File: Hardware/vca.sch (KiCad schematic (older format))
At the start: 0 parts

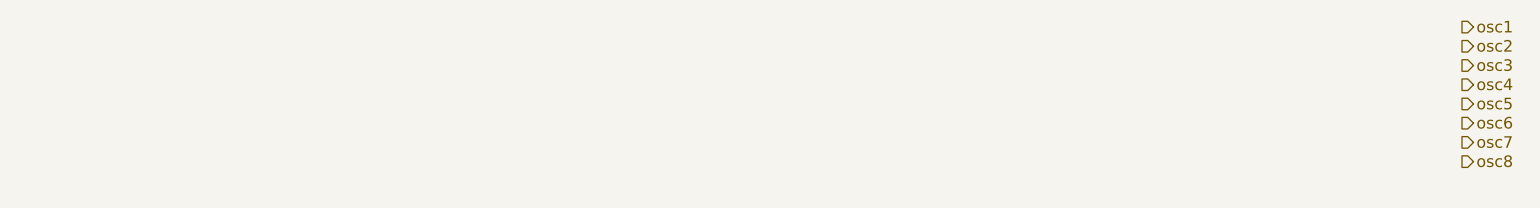
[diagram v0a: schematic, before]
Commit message: add sheets for the remaining functionality. This should hopefully be all sheets, but might add more if necessary.
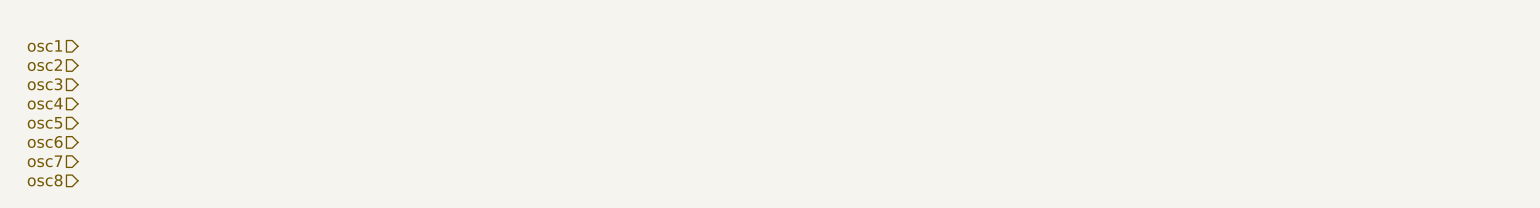
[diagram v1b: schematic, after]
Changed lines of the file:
@@
 $Descr A4 11693 8268
 encoding utf-8
-Sheet 2 7
+Sheet 5 7
 Title ""
 Date ""
@@
 Comment4 ""
 $EndDescr
-Text HLabel 9050 1900 2    60   Output ~ 0
+Text HLabel 1850 2000 0    60   Input ~ 0
 osc1
-Text HLabel 9050 2000 2    60   Output ~ 0
+Text HLabel 1850 2100 0    60   Input ~ 0
 osc2
-Text HLabel 9050 2100 2    60   Output ~ 0
+Text HLabel 1850 2200 0    60   Input ~ 0
 osc3
-Text HLabel 9050 2200 2    60   Output ~ 0
+Text HLabel 1850 2300 0    60   Input ~ 0
 osc4
-Text HLabel 9050 2300 2    60   Output ~ 0
+Text HLabel 1850 2400 0    60   Input ~ 0
 osc5
-Text HLabel 9050 2400 2    60   Output ~ 0
+Text HLabel 1850 2500 0    60   Input ~ 0
 osc6
-Text HLabel 9050 2500 2    60   Output ~ 0
+Text HLabel 1850 2600 0    60   Input ~ 0
 osc7
-Text HLabel 9050 2600 2    60   Output ~ 0
+Text HLabel 1850 2700 0    60   Input ~ 0
 osc8
 $EndSCHEMATC

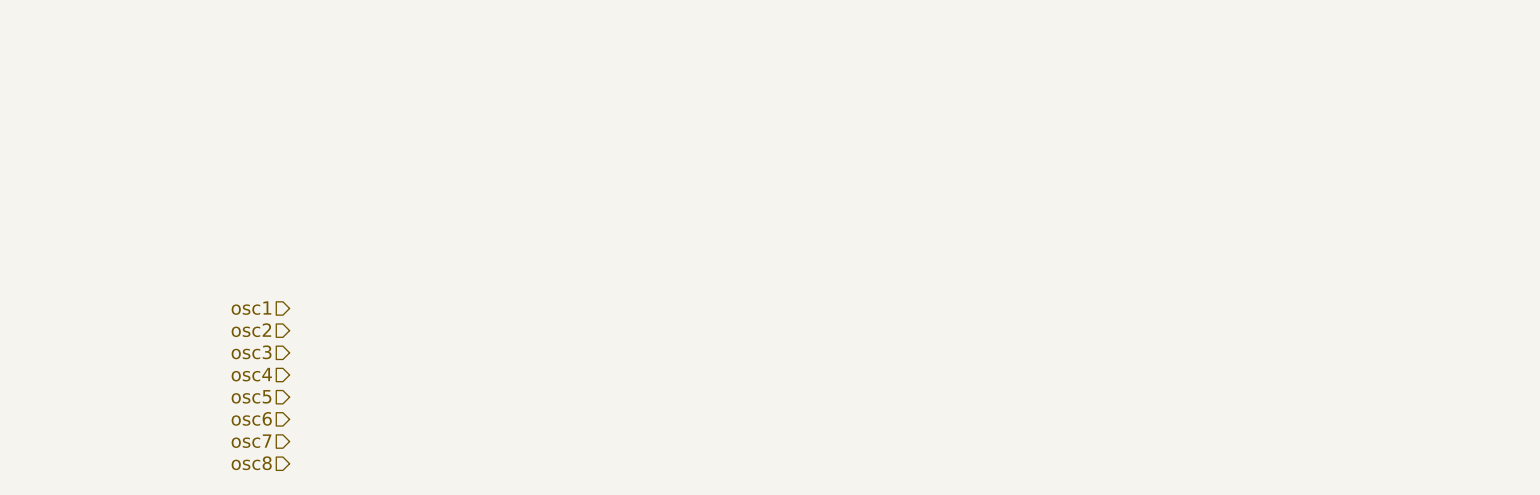
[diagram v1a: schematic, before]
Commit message: add basic version of VCA for one channel
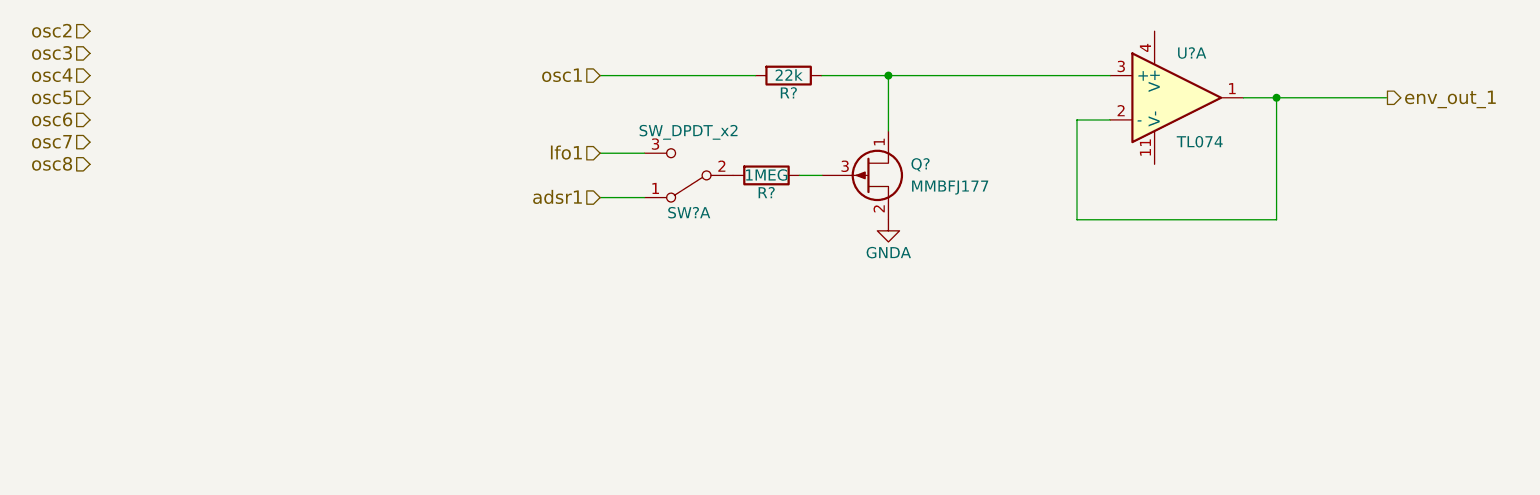
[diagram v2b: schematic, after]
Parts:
- added Q?: MMBFJ177, symbol Q_PJFET_DSG
- added R?: 22k, symbol R
- added R?: 1MEG, symbol R
- added SW?: SW_DPDT_x2, symbol SW_DPDT_x2
- added U?: TL074, symbol TL074
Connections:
- net osc1: now also R?.2
- new net: Q?.1 (D), R?.1, U?.3 (+)
- new net: Q?.3 (G), R?.1
- new net: R?.2, SW?.2 (B)
- new net GNDA: Q?.2 (S)
- new net adsr1: SW?.1 (A)
- new net env_out_1: U?.1, U?.2 (-)
- new net lfo1: SW?.3 (C)
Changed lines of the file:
@@
 $Descr A4 11693 8268
 encoding utf-8
-Sheet 5 7
+Sheet 5 8
 Title ""
 Date ""
@@
 Comment4 ""
 $EndDescr
-Text HLabel 1850 2000 0    60   Input ~ 0
+Text HLabel 3250 950  0    60   Input ~ 0
 osc1
-Text HLabel 1850 2100 0    60   Input ~ 0
+Text HLabel 950  750  0    60   Input ~ 0
 osc2
-Text HLabel 1850 2200 0    60   Input ~ 0
+Text HLabel 950  850  0    60   Input ~ 0
 osc3
-Text HLabel 1850 2300 0    60   Input ~ 0
+Text HLabel 950  950  0    60   Input ~ 0
 osc4
-Text HLabel 1850 2400 0    60   Input ~ 0
+Text HLabel 950  1050 0    60   Input ~ 0
 osc5
-Text HLabel 1850 2500 0    60   Input ~ 0
+Text HLabel 950  1150 0    60   Input ~ 0
 osc6
-Text HLabel 1850 2600 0    60   Input ~ 0
+Text HLabel 950  1250 0    60   Input ~ 0
 osc7
-Text HLabel 1850 2700 0    60   Input ~ 0
+Text HLabel 950  1350 0    60   Input ~ 0
 osc8
+$Comp
+L Q_PJFET_DSG Q?
+U 1 1 5C359797
+P 4450 1400
+F 0 "Q?" H 4650 1450 50  0000 L CNN
+F 1 "MMBFJ177" H 4650 1350 50  0000 L CNN
+F 2 "" H 4650 1500 50  0001 C CNN
+F 3 "" H 4450 1400 50  0001 C CNN
+	1    4450 1400
+	1    0    0    -1
+$EndComp
+$Comp
+L R R?
+U 1 1 5C359814
+P 4100 950
+F 0 "R?" V 4180 950 50  0000 C CNN
+F 1 "22k" V 4100 950 50  0000 C CNN
+F 2 "" V 4030 950 50  0001 C CNN
+F 3 "" H 4100 950 50  0001 C CNN
+	1    4100 950
+	0    1    1    0
+$EndComp
+$Comp
+L TL074 U?
+U 1 1 5C359D57
+P 5850 1050
+F 0 "U?" H 5850 1250 50  0000 L CNN
+F 1 "TL074" H 5850 850 50  0000 L CNN
+F 2 "" H 5800 1150 50  0001 C CNN
+F 3 "" H 5900 1250 50  0001 C CNN
+	1    5850 1050
+	1    0    0    -1
+$EndComp
+Wire Wire Line
+	6150 1050 6300 1050
+Wire Wire Line
+	6300 1050 6800 1050
+Wire Wire Line
+	6300 1050 6300 1600
+Wire Wire Line
+	6300 1600 5400 1600
+Wire Wire Line
+	5400 1600 5400 1150
+Wire Wire Line
+	5400 1150 5550 1150
+$Comp
+L GNDA #PWR?
+U 1 1 5C359DD5
+P 4550 1600
+F 0 "#PWR?" H 4550 1350 50  0001 C CNN
+F 1 "GNDA" H 4550 1450 50  0000 C CNN
+F 2 "" H 4550 1600 50  0001 C CNN
+F 3 "" H 4550 1600 50  0001 C CNN
+	1    4550 1600
+	1    0    0    -1
+$EndComp
+Wire Wire Line
+	4250 950  4550 950
+Wire Wire Line
+	4550 950  5550 950
+Wire Wire Line
+	3950 950  3250 950
+Wire Wire Line
+	4550 1200 4550 950
+$Comp
+L R R?
+U 1 1 5C359EAD
+P 4000 1400
+F 0 "R?" V 4080 1400 50  0000 C CNN
+F 1 "1MEG" V 4000 1400 50  0000 C CNN
+F 2 "" V 3930 1400 50  0001 C CNN
+F 3 "" H 4000 1400 50  0001 C CNN
+	1    4000 1400
+	0    1    1    0
+$EndComp
+Wire Wire Line
+	4150 1400 4250 1400
+Connection ~ 4550 950
+Text HLabel 3250 1300 0    60   Input ~ 0
+lfo1
+Text HLabel 3250 1500 0    60   Input ~ 0
+adsr1
+$Comp
+L SW_DPDT_x2 SW?
+U 1 1 5C35A0BC
+P 3650 1400
+F 0 "SW?" H 3650 1570 50  0000 C CNN
+F 1 "SW_DPDT_x2" H 3650 1200 50  0000 C CNN
+F 2 "" H 3650 1400 50  0001 C CNN
+F 3 "" H 3650 1400 50  0001 C CNN
+	1    3650 1400
+	-1   0    0    1
+$EndComp
+Wire Wire Line
+	3250 1300 3450 1300
+Wire Wire Line
+	3250 1500 3450 1500
+Text HLabel 6800 1050 2    60   Output ~ 0
+env_out_1
+Connection ~ 6300 1050
 $EndSCHEMATC

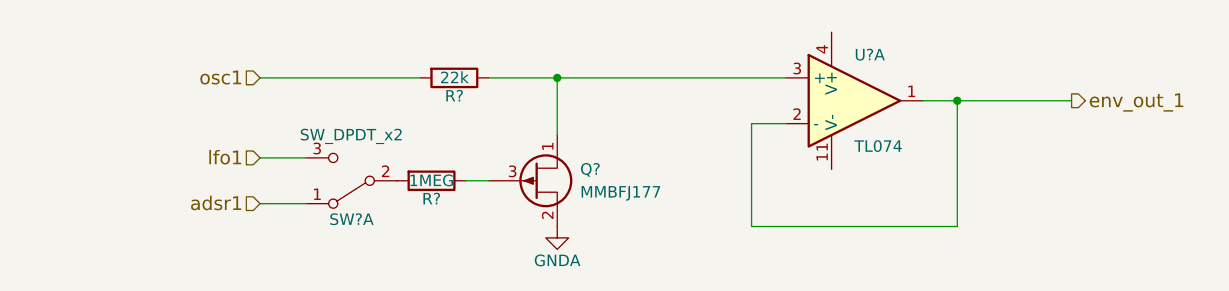
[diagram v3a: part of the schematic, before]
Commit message: add bill of materials spreadsheet and begin to populate with values
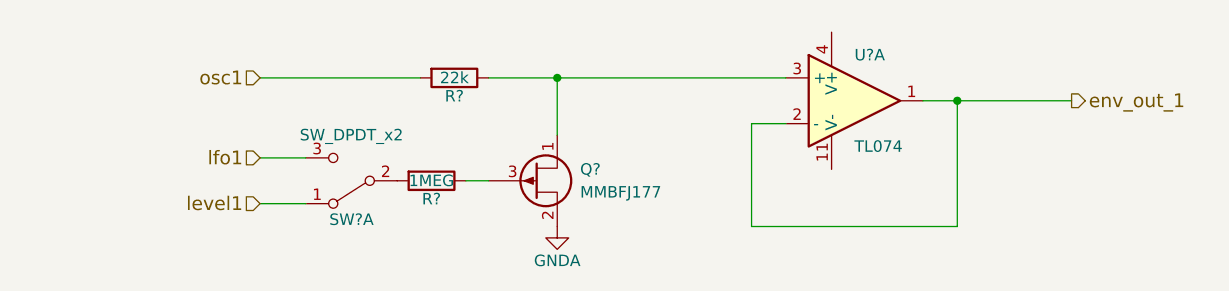
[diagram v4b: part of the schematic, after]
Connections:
- net adsr1 renamed level1
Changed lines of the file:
@@
 $EndComp
 Wire Wire Line
-	6150 1050 6300 1050
-Wire Wire Line
-	6300 1050 6800 1050
+	6150 1050 6800 1050
 Wire Wire Line
 	6300 1050 6300 1600
@@
 $EndComp
 Wire Wire Line
-	4250 950  4550 950
-Wire Wire Line
-	4550 950  5550 950
+	4250 950  5550 950
 Wire Wire Line
 	3950 950  3250 950
@@
 lfo1
 Text HLabel 3250 1500 0    60   Input ~ 0
-adsr1
+level1
 $Comp
 L SW_DPDT_x2 SW?

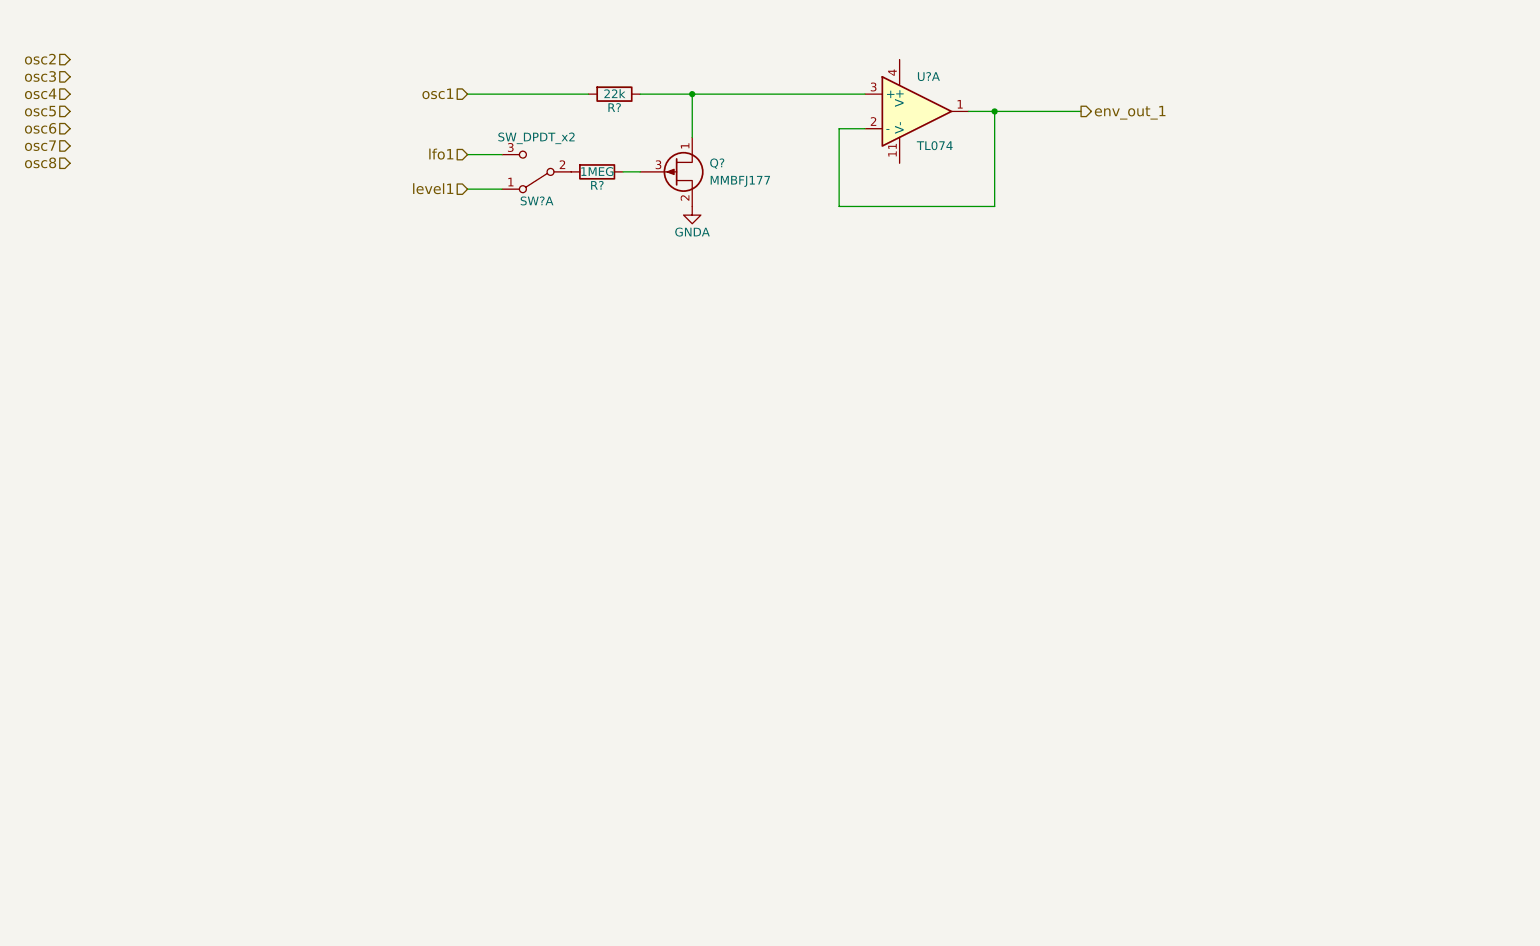
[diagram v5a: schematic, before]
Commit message: complete wiring of top level schematic hierarchical pages
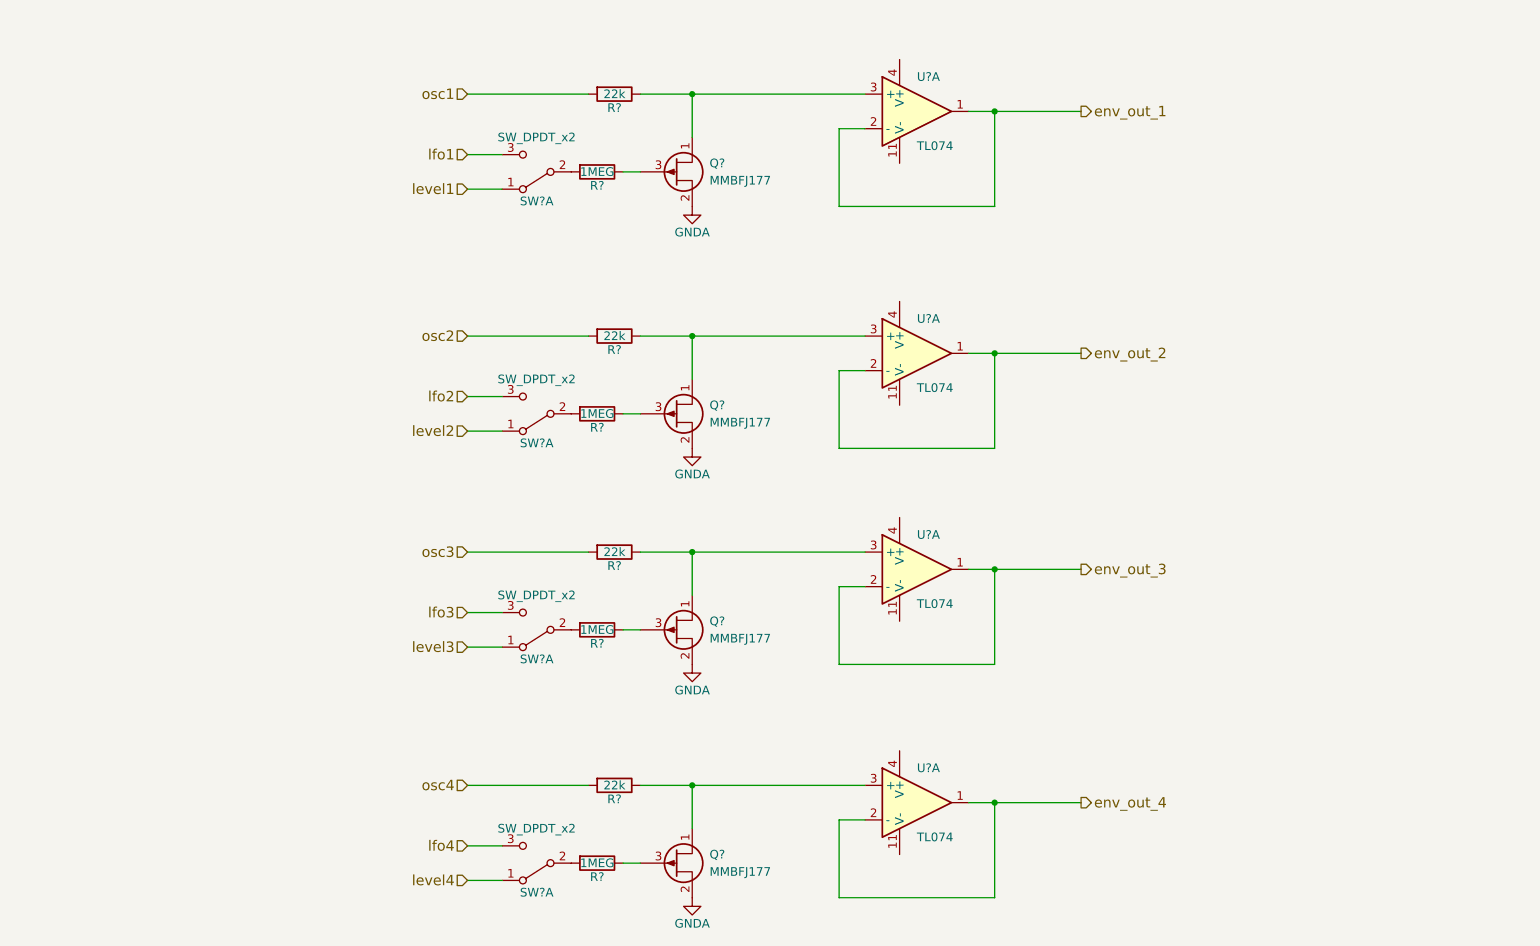
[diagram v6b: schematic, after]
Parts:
- added Q? (x3): MMBFJ177, symbol Q_PJFET_DSG
- added R? (x3): 22k, symbol R
- added R? (x3): 1MEG, symbol R
- added SW? (x3): SW_DPDT_x2, symbol SW_DPDT_x2
- added U? (x3): TL074, symbol TL074
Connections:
- net GNDA: now also Q?.2 (S), Q?.2 (S), Q?.2 (S)
- net osc2: now also R?.2
- net osc3: now also R?.2
- net osc4: now also R?.2
- new net: Q?.1 (D), R?.1, U?.3 (+) (x3)
- new net: Q?.3 (G), R?.1 (x3)
- new net: R?.2, SW?.2 (B) (x3)
- new net env_out_2: U?.1, U?.2 (-)
- new net env_out_3: U?.1, U?.2 (-)
- new net env_out_4: U?.1, U?.2 (-)
- new net level2: SW?.1 (A)
- new net level3: SW?.1 (A)
- new net level4: SW?.1 (A)
- new net lfo2: SW?.3 (C)
- new net lfo3: SW?.3 (C)
- new net lfo4: SW?.3 (C)
